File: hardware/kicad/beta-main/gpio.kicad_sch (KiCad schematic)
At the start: 1 part

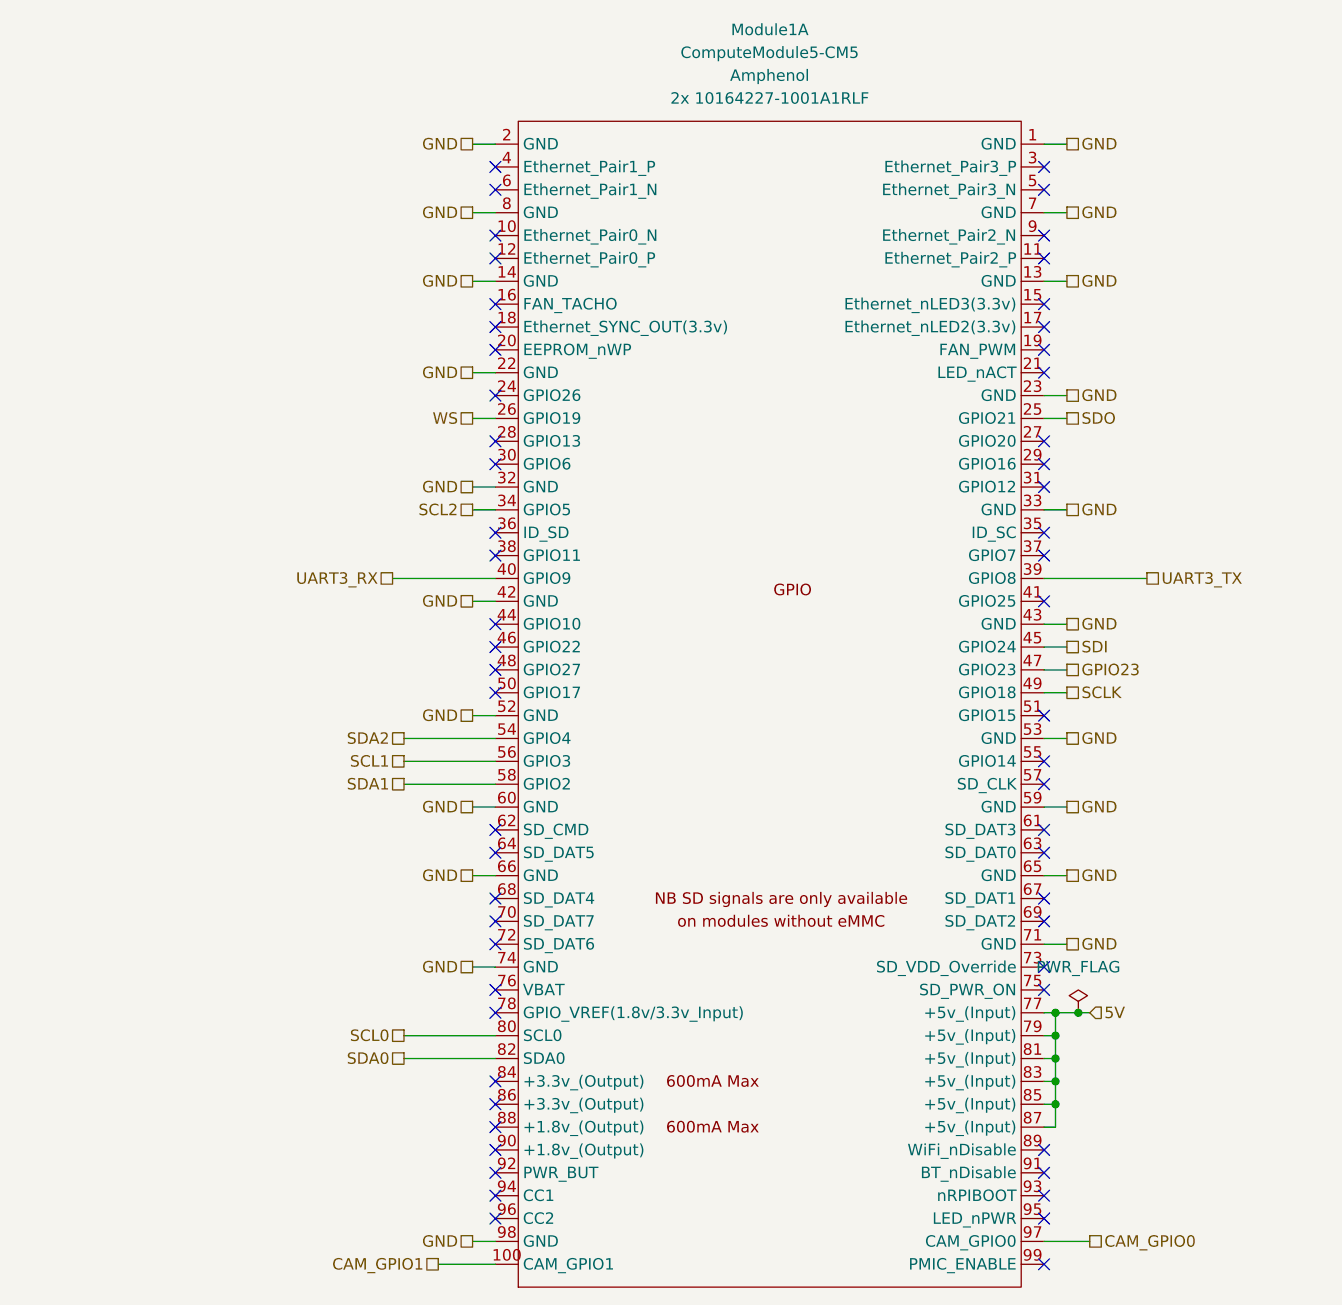
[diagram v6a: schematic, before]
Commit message: remove power symbols from hierarchy and move different subsystems  around
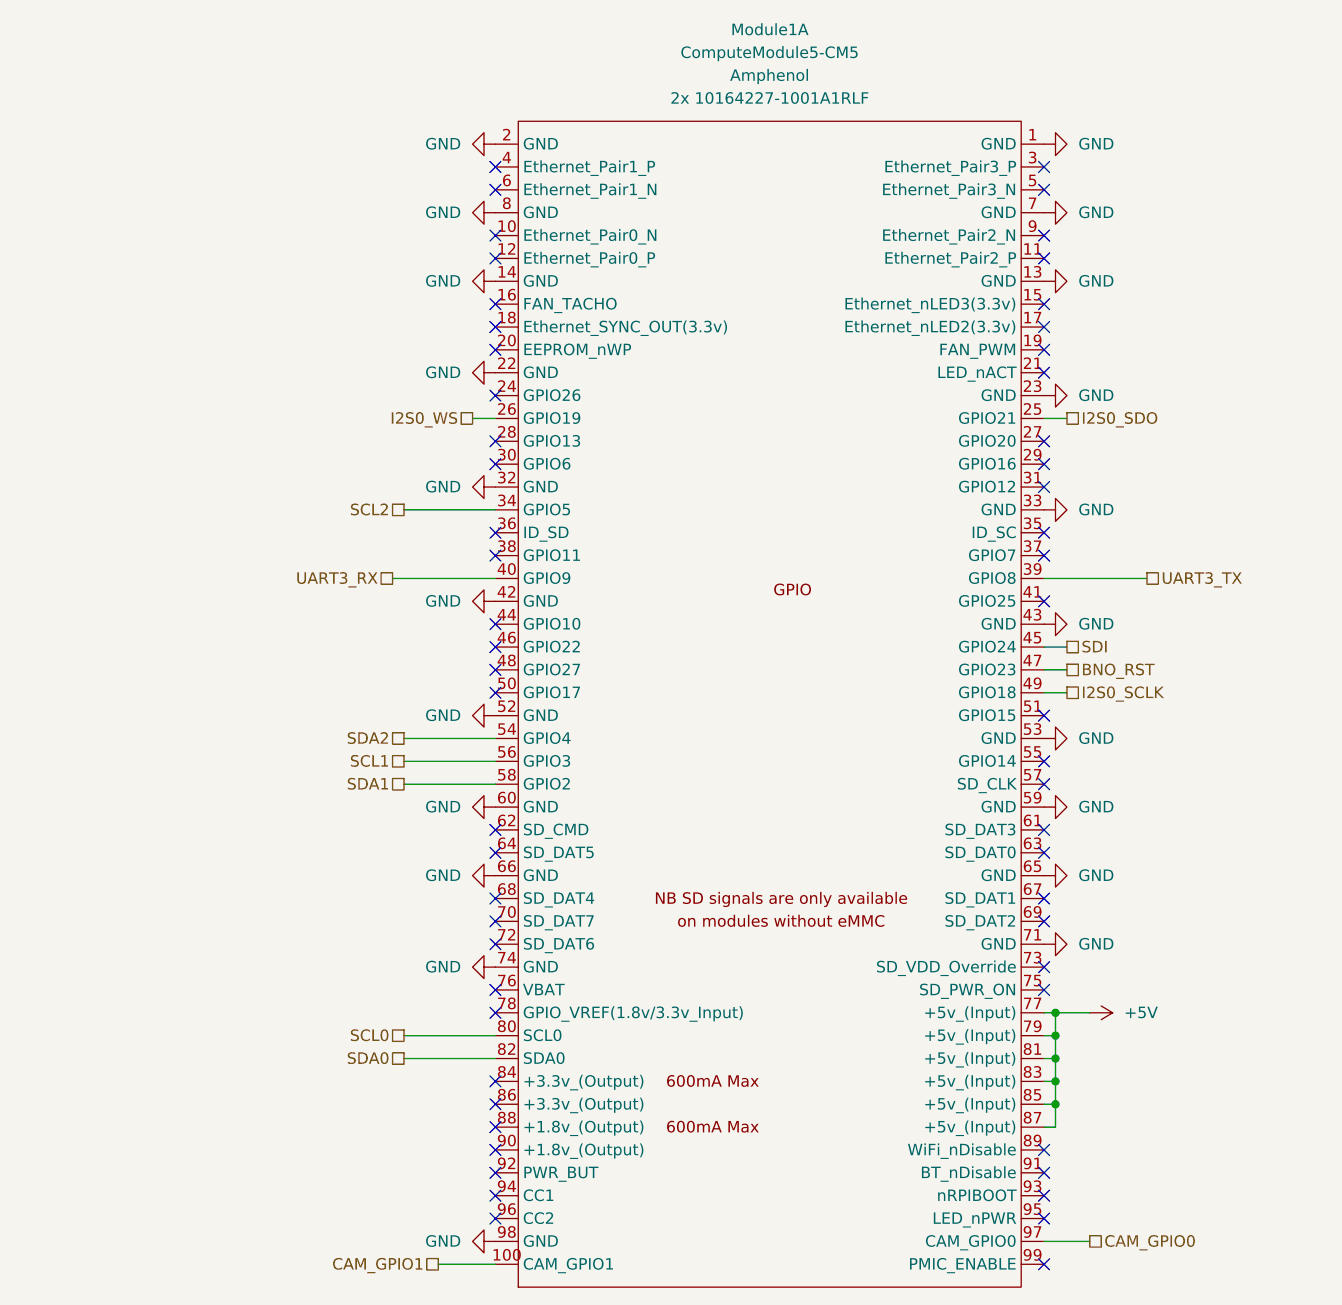
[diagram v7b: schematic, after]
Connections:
- net 5V renamed +5V
- net GPIO23 renamed BNO_RST
- net SCLK renamed I2S0_SCLK
- net SDO renamed I2S0_SDO
- net WS renamed I2S0_WS

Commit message: add modifications
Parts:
- removed Module1: ComputeModule5-CM5, CM5IO:Raspberry-Pi-5-Compute-Module, symbol CM5IO:ComputeModule5-CM5
- added CM5: ComputeModule5-CM5, CM5IO:Raspberry-Pi-5-Compute-Module, symbol CM5IO:ComputeModule5-CM5
- added D1: LED_RED, LED_SMD:LED_0603_1608Metric, symbol Device:LED_Small
- added R12: 1k, Resistor_SMD:R_0603_1608Metric, symbol Device:R_Small
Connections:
- net +5V: now also CM5.77 (+5v_(Input)), CM5.79 (+5v_(Input)), CM5.81 (+5v_(Input)), CM5.83 (+5v_(Input)), CM5.85 (+5v_(Input)), CM5.87 (+5v_(Input))
- net BNO_RST: now also CM5.47 (GPIO23)
- net CAM_GPIO0: now also CM5.97 (CAM_GPIO0)
- net CAM_GPIO1: now also CM5.100 (CAM_GPIO1)
- net GND: now also CM5.1 (GND), CM5.13 (GND), CM5.14 (GND), CM5.2 (GND), CM5.22 (GND), CM5.23 (GND), CM5.32 (GND), CM5.33 (GND), CM5.42 (GND), CM5.43 (GND), CM5.52 (GND), CM5.53 (GND), CM5.59 (GND), CM5.60 (GND), CM5.65 (GND), CM5.66 (GND), CM5.7 (GND), CM5.71 (GND), CM5.74 (GND), CM5.8 (GND), CM5.98 (GND)
- net I2S0_SCLK: now also CM5.49 (GPIO18)
- net I2S0_SDO: now also CM5.25 (GPIO21)
- net I2S0_WS: now also CM5.26 (GPIO19)
- net SDI: now also CM5.45 (GPIO24)
- net UART3_RX: now also CM5.40 (GPIO9)
- net UART3_TX: now also CM5.39 (GPIO8)
- new net: D1.1 (K), R12.1
- new net: CM5.21 (LED_nACT), R12.2
- new net +3V3: CM5.78 (GPIO_VREF(1.8v/3.3v_Input)), D1.2 (A)
- new net FAN_PWM: CM5.19 (FAN_PWM)
- new net I2C0_SCL: CM5.80 (SCL0)
- new net I2C0_SDA: CM5.82 (SDA0)
- new net I2C1_SCL: CM5.56 (GPIO3)
- new net I2C1_SDA: CM5.58 (GPIO2)
- new net I2C2_SCL: CM5.34 (GPIO5)
- new net I2C2_SDA: CM5.54 (GPIO4)
- new net I2C3_SCL: CM5.37 (GPIO7)
- new net I2C3_SDA: CM5.30 (GPIO6)
- new net PWR_BUT: CM5.92 (PWR_BUT)
- no-connect marks 58 -> 52
